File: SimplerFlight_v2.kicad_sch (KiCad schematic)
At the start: 18 parts

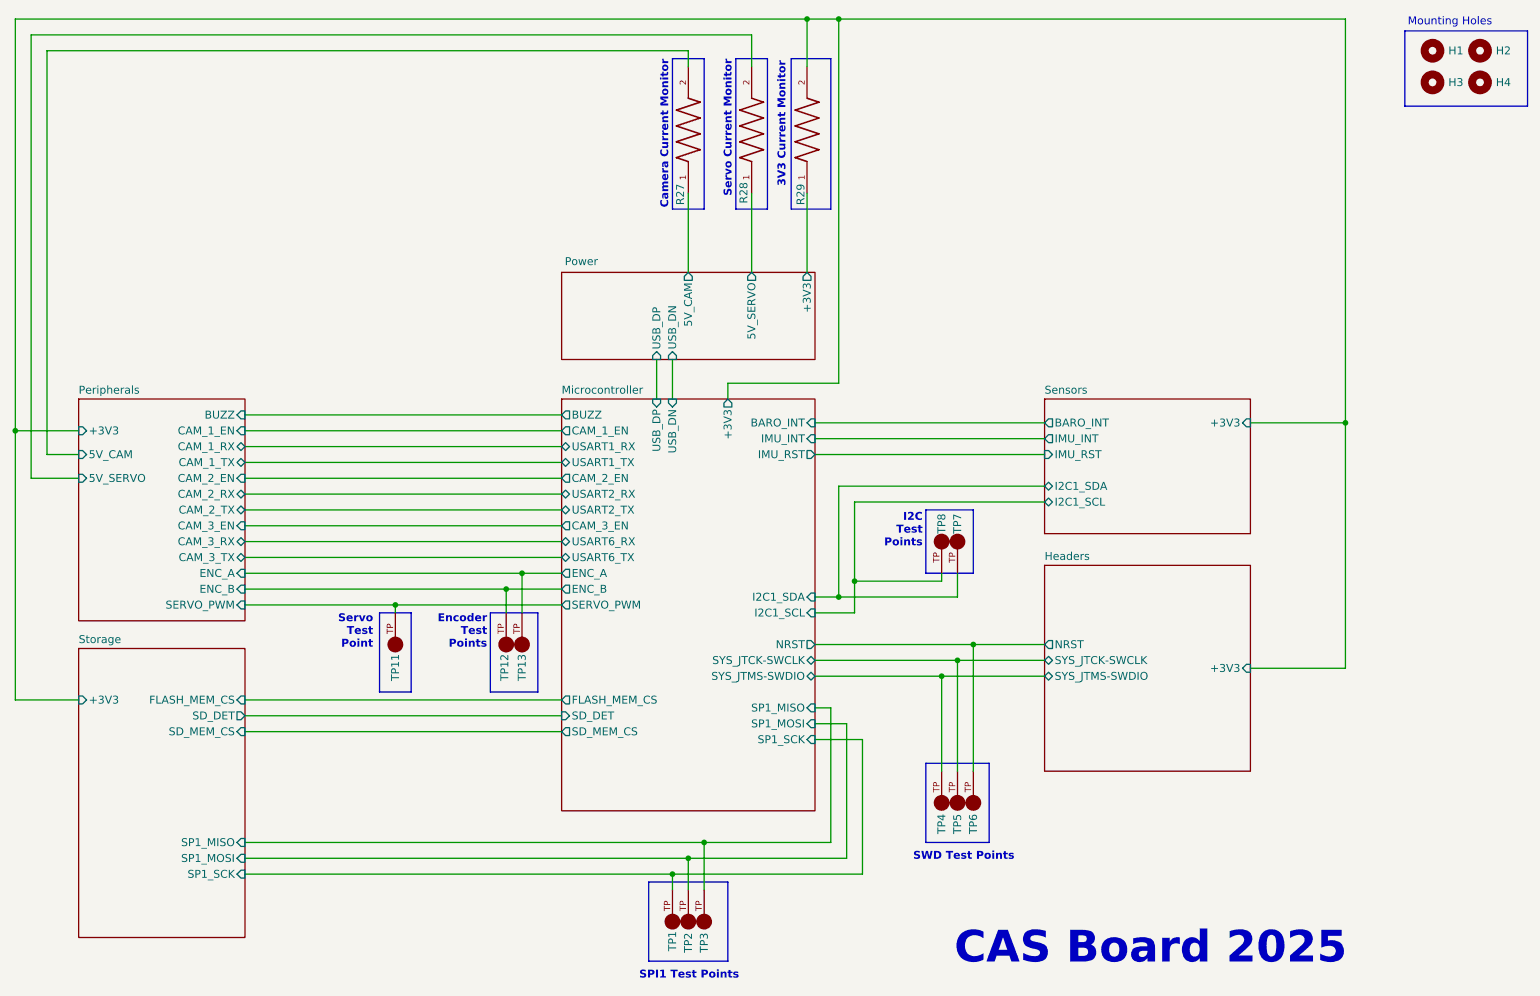
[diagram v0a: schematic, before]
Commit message: remove camera power and interface headers and pins from schematic and PCB
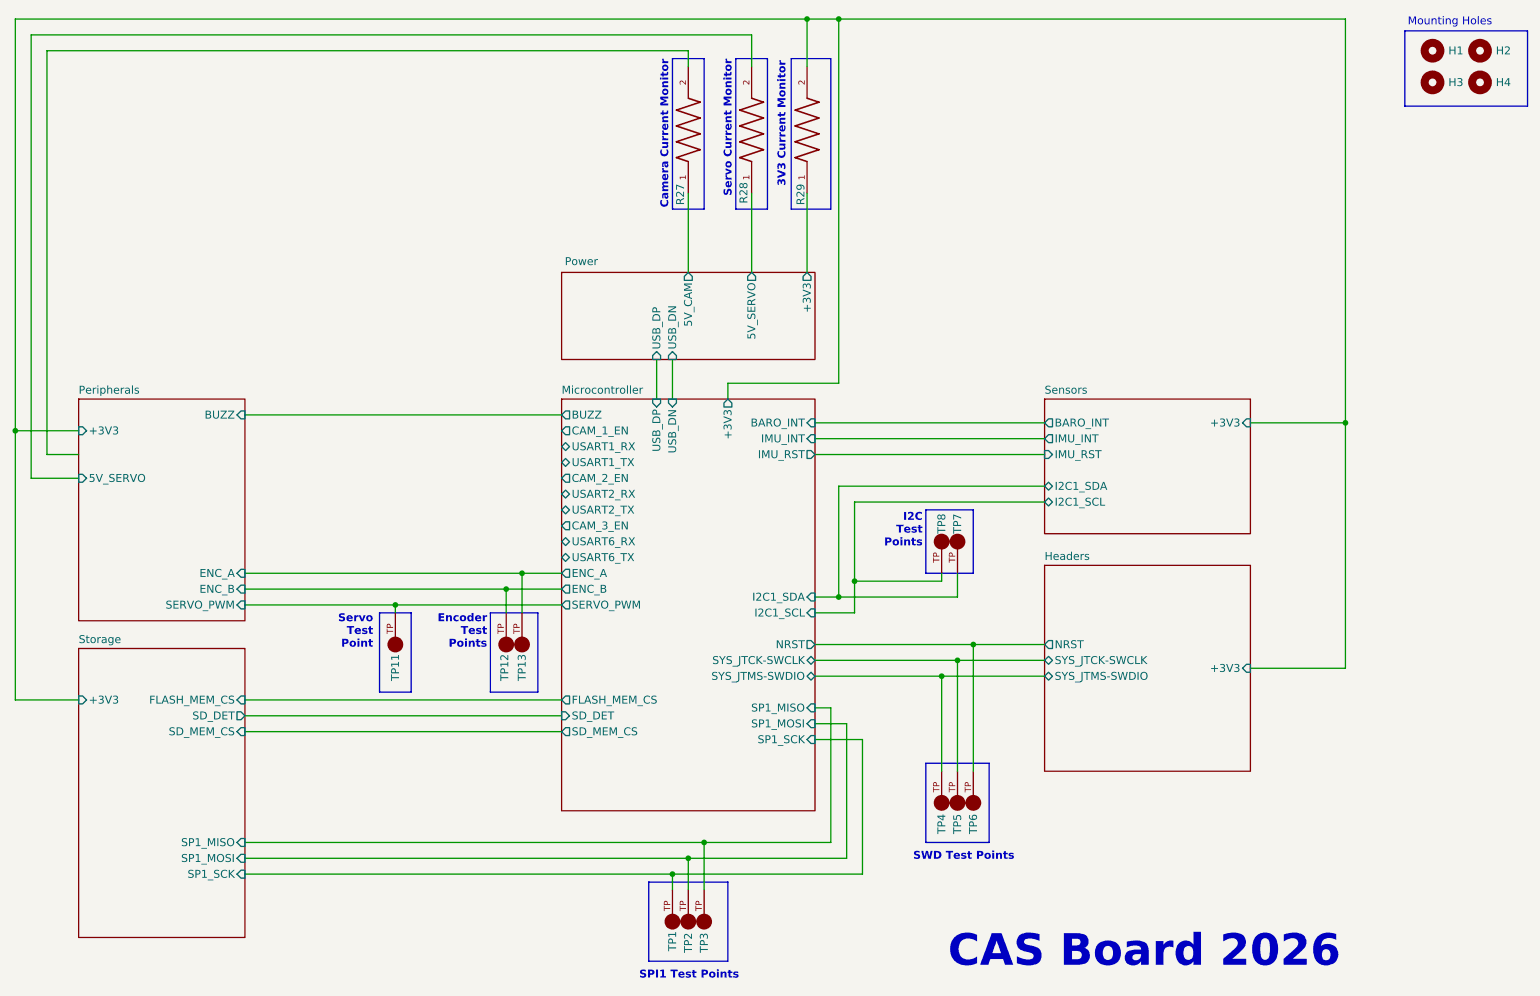
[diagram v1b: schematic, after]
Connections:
- net Peripherals/5V_CAM: no longer names the net of R27.2
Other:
- sheet Peripherals ports: added none; removed 5V_CAM, CAM_1_EN, CAM_1_RX, CAM_1_TX, CAM_2_EN, CAM_2_RX, CAM_2_TX, CAM_3_EN, CAM_3_RX, CAM_3_TX
- note added: "CAS Board 2026"
- note removed: "CAS Board 2025"
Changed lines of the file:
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@@
 		)
 	)
-	(text "CAS Board 2025\n\n"
+	(text "CAS Board 2026"
 		(exclude_from_sim no)
-		(at 210.058 177.292 0)
+		(at 209.042 173.736 0)
 		(effects
 			(font
@@
 	(wire
 		(pts
-			(xy 64.77 110.49) (xy 115.57 110.49)
-		)
-		(stroke
-			(width 0)
-			(type default)
-		)
-	)
-	(wire
-		(pts
 			(xy 64.77 118.11) (xy 88.9 118.11)
 		)
@@
 		)
 	)
-	(wire
-		(pts
-			(xy 64.77 97.79) (xy 115.57 97.79)
-		)
-		(stroke
-			(width 0)
-			(type default)
-		)
-	)
 	(polyline
 		(pts
@@
 		)
 	)
-	(wire
-		(pts
-			(xy 64.77 92.71) (xy 115.57 92.71)
-		)
-		(stroke
-			(width 0)
-			(type default)
-		)
-	)
 	(polyline
 		(pts
@@
 	(wire
 		(pts
-			(xy 64.77 100.33) (xy 115.57 100.33)
-		)
-		(stroke
-			(width 0)
-			(type default)
-		)
-	)
-	(wire
-		(pts
 			(xy 133.35 161.29) (xy 133.35 163.83)
 		)
@@
 	(wire
 		(pts
-			(xy 64.77 107.95) (xy 115.57 107.95)
-		)
-		(stroke
-			(width 0)
-			(type default)
-		)
-	)
-	(wire
-		(pts
 			(xy 156.21 88.9) (xy 193.04 88.9)
 		)
@@
 	(wire
 		(pts
-			(xy 64.77 90.17) (xy 115.57 90.17)
-		)
-		(stroke
-			(width 0)
-			(type default)
-		)
-	)
-	(wire
-		(pts
 			(xy 146.05 26.67) (xy 146.05 31.75)
 		)
@@
 	(wire
 		(pts
-			(xy 64.77 105.41) (xy 115.57 105.41)
-		)
-		(stroke
-			(width 0)
-			(type default)
-		)
-	)
-	(wire
-		(pts
 			(xy 109.22 113.03) (xy 115.57 113.03)
 		)
@@
 		)
 	)
-	(wire
-		(pts
-			(xy 64.77 102.87) (xy 115.57 102.87)
-		)
-		(stroke
-			(width 0)
-			(type default)
-		)
-	)
 	(polyline
 		(pts
@@
 	(wire
 		(pts
-			(xy 64.77 95.25) (xy 115.57 95.25)
-		)
-		(stroke
-			(width 0)
-			(type default)
-		)
-	)
-	(wire
-		(pts
 			(xy 64.77 158.75) (xy 135.89 158.75)
 		)
@@
 			)
 		)
-		(pin "CAM_1_EN" input
-			(at 64.77 90.17 0)
-			(effects
-				(font
-					(size 1.27 1.27)
-				)
-				(justify right)
-			)
-		)
-		(pin "CAM_1_RX" bidirectional
-			(at 64.77 92.71 0)
-			(effects
-				(font
-					(size 1.27 1.27)
-				)
-				(justify right)
-			)
-		)
-		(pin "CAM_1_TX" bidirectional
-			(at 64.77 95.25 0)
-			(effects
-				(font
-					(size 1.27 1.27)
-				)
-				(justify right)
-			)
-		)
-		(pin "CAM_2_EN" input
-			(at 64.77 97.79 0)
-			(effects
-				(font
-					(size 1.27 1.27)
-				)
-				(justify right)
-			)
-		)
-		(pin "CAM_2_RX" bidirectional
-			(at 64.77 100.33 0)
-			(effects
-				(font
-					(size 1.27 1.27)
-				)
-				(justify right)
-			)
-		)
-		(pin "CAM_2_TX" bidirectional
-			(at 64.77 102.87 0)
-			(effects
-				(font
-					(size 1.27 1.27)
-				)
-				(justify right)
-			)
-		)
-		(pin "CAM_3_EN" input
-			(at 64.77 105.41 0)
-			(effects
-				(font
-					(size 1.27 1.27)
-				)
-				(justify right)
-			)
-		)
-		(pin "CAM_3_RX" bidirectional
-			(at 64.77 107.95 0)
-			(effects
-				(font
-					(size 1.27 1.27)
-				)
-				(justify right)
-			)
-		)
-		(pin "CAM_3_TX" bidirectional
-			(at 64.77 110.49 0)
-			(effects
-				(font
-					(size 1.27 1.27)
-				)
-				(justify right)
-			)
-		)
 		(pin "ENC_A" input
 			(at 64.77 113.03 0)
@@
 			(effects
 				(font
-					(size 1.27 1.27)
-				)
-				(justify left)
-			)
-		)
-		(pin "5V_CAM" input
-			(at 38.1 93.98 180)
-			(effects
-				(font
